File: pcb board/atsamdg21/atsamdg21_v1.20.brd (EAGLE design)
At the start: 100 x 80 mm, 54 parts, among them IC1 DS3231MZ+, IC2 TPS22810TDBVRQ1, SW1 SPST_TACT-KMR2, U1 ATSAMD21G18A-AU, U2 AP2112K-3.3, U4 RFM69HCW, X1 TSW-105-07-G-S, X2 32.768, X3 microUSB, X4 uFL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

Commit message: update 05/15
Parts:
- moved BATTERY 88.5 mm to (3.81, 24.6), turned to 90 degrees
- moved C10 82.8 mm to (9.91, 38.6), turned to 90 degrees
- moved C14 80.6 mm to (12.2, 38.6), turned to 90 degrees
- moved SOLAR 80.0 mm to (3.81, 30.7), turned to 270 degrees
- moved C9 74.2 mm to (54.9, 2.03), turned to 270 degrees
- moved POWER 73.9 mm to (12.2, 47.2), turned to 180 degrees
- moved TRIGGER 69.9 mm to (18.8, 47.2), turned to 180 degrees
- moved R4 69.0 mm to (61.7, 10.4), flipped to the bottom, turned to 270 degrees
- moved C3 62.4 mm to (63.0, 32.3), turned to 270 degrees
- moved IC2 58.3 mm to (42.9, 43.7), turned to 90 degrees
- moved C5 57.5 mm to (52.8, 41.1)
- moved IC1 57.0 mm to (67.1, 10.7), flipped to the bottom, turned to 180 degrees
- moved R7 56.9 mm to (62.0, 26.4), turned to 270 degrees
- moved C1 53.7 mm to (51.8, 38.6), turned to 270 degrees
- moved C7 52.7 mm to (48.8, 24.1)
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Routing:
- net 12VIN: track 0.00 -> 83.2 mm
- net RAIN_G: track 0.00 -> 62.5 mm, vias 0 -> 2
- net A0: track 0.00 -> 58.1 mm, vias 0 -> 1
- net DUETRIG: track 0.00 -> 52.4 mm, vias 0 -> 2
- net D10: track 0.00 -> 48.1 mm
- net D11: track 0.00 -> 42.3 mm
- net USB_D+: track 0.00 -> 38.2 mm, vias 0 -> 2
- net USB_D-: track 0.00 -> 37.8 mm, vias 0 -> 2
- net BATT: track 0.00 -> 34.8 mm
- net N$6: track 0.00 -> 22.9 mm
- net +4V: track 0.00 -> 22.1 mm, vias 0 -> 1
- net SWDIO: track 0.00 -> 20.1 mm
- net TX: track 0.00 -> 19.3 mm, vias 0 -> 1
- net SWCLK: track 0.00 -> 18.5 mm
- net RX: track 0.00 -> 17.4 mm, vias 0 -> 1
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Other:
- board size 100 x 80 mm -> 106.6 x 57.1 mm

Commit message: 05/22 update
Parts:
- moved C11 42.6 mm to (27.2, 11.9), turned to 90 degrees
- moved R10 42.4 mm to (30.2, 10.9)
- moved D1 42.4 mm to (31.2, 8.38)
- moved U2 42.1 mm to (30.2, 14.7)
- moved G1 27.7 mm to (59.9, 12.7), turned to 270 degrees
- moved R4 25.0 mm to (69.1, 34.3), flipped to the top, turned to 0 degrees
- moved C17 23.2 mm to (24.1, 39.6), turned to 270 degrees
- moved C16 23.0 mm to (20.1, 34.3), turned to 90 degrees
- moved IC1 22.7 mm to (64.5, 33.3), flipped to the top, turned to 270 degrees
- moved IC2 22.4 mm to (21.1, 38.6)
- moved SW1 17.6 mm to (49.8, 43.4), turned to 180 degrees
- moved R6 15.0 mm to (33.0, 33.0), turned to 180 degrees
- moved X6 14.0 mm to (57.1, 43.7), turned to 0 degrees
- moved C13 12.4 mm to (45.0, 43.2)
- moved C12 12.4 mm to (45.0, 46.5)
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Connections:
- removed net N$3: R3.2, U1.40
- removed net N$8: C17.1
- net !RESET: now also R3.2, U1.40
- net N$6: now also C17.1
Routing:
- net GND: track 0.00 -> 412.4 mm, vias 0 -> 8
- net +3V3: track 9.57 -> 197.1 mm, vias 0 -> 5
- net VBUS: track 16.6 -> 99.1 mm, vias 0 -> 2
- net N$2: track 0.00 -> 19.3 mm, vias 0 -> 1
- net USB_D+: track 38.2 -> 21.0 mm, vias 2 -> 1
- net USB_D-: track 37.8 -> 21.3 mm, vias 2 -> 1
- net !RESET: track 4.00 -> 16.7 mm, vias 0 -> 2
- net VOLT_SENS: track 12.2 -> 24.6 mm, vias 0 -> 2
- net N$6: track 22.9 -> 12.7 mm
- net D11: track 42.3 -> 33.1 mm, vias 0 -> 2
- net 12VIN: track 83.2 -> 74.9 mm
- net N$7: track 7.90 -> 16.0 mm
- net SCK: track 12.8 -> 4.97 mm
- net RAIN_G: track 62.5 -> 54.8 mm, vias 2 -> 4
- net D10: track 48.1 -> 40.8 mm, vias 0 -> 2
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- added copper zone on layer 1, net GND
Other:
- board size 106.6 x 57.1 mm -> 71.8 x 51.6 mm

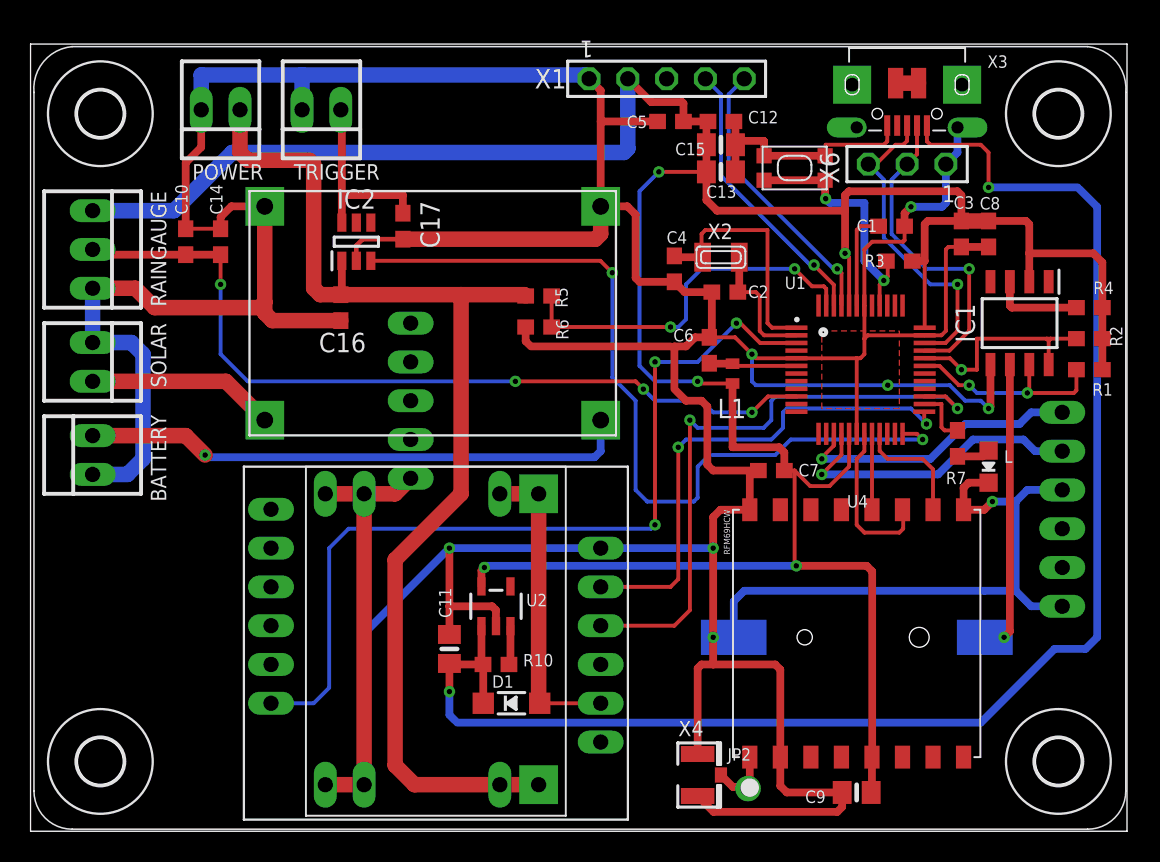
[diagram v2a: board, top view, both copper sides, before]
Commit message: -updated usb pin connections, overlap, ground plane bottom
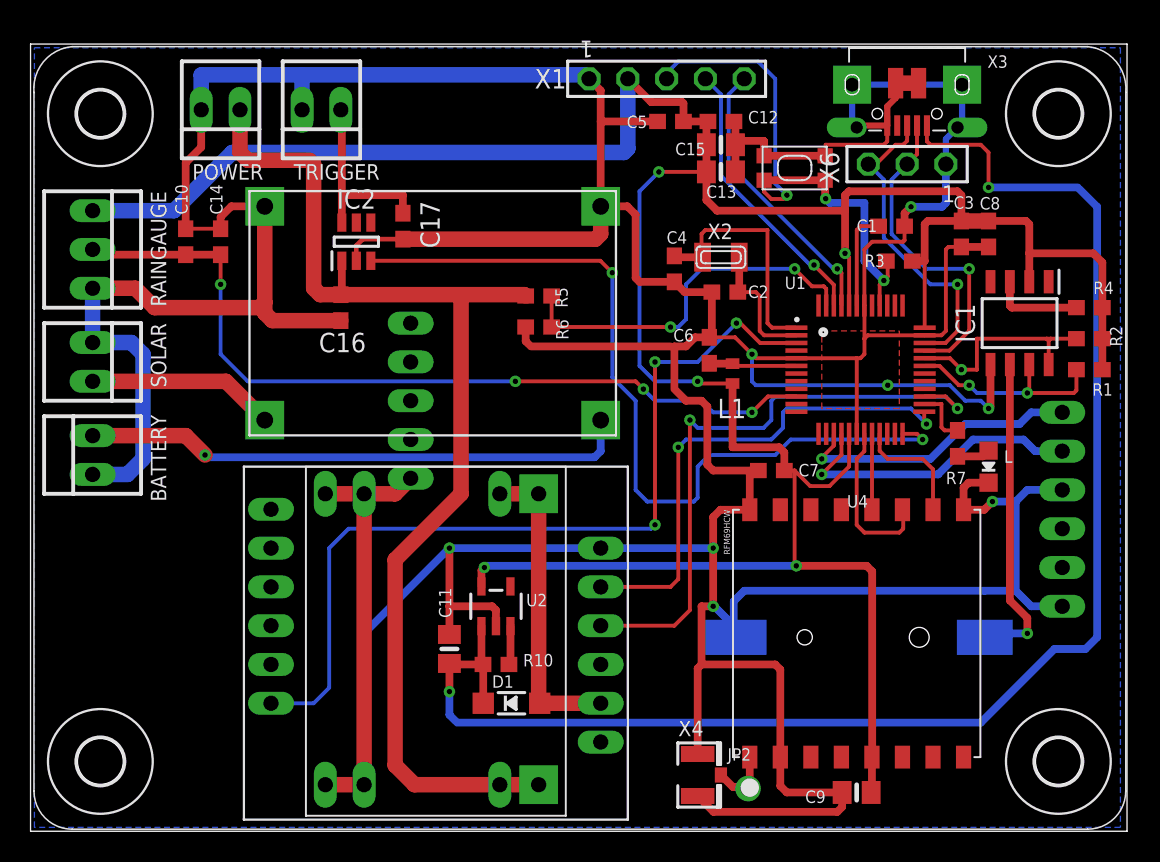
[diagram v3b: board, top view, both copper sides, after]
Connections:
- removed net RST: X1.3
- net !RESET: now also X1.3
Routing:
- net GND: track 412.4 -> 432.6 mm
- net !RESET: track 16.7 -> 35.6 mm, vias 2 -> 3
- net N$2: track 19.3 -> 21.0 mm
- added copper zone on layer 16, net GND
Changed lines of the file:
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@@
 <?xml version="1.0" encoding="utf-8"?>
 <!DOCTYPE eagle SYSTEM "eagle.dtd">
-<eagle version="9.6.1">
+<eagle version="9.5.1">
 <drawing>
 <settings>
@@
 <contactref element="U1" pad="35"/>
 <contactref element="U1" pad="42"/>
-<via x="44.45" y="12.7" extent="1-16" drill="0.35"/>
-<wire x1="44.45" y1="12.7" x2="45.7982" y2="12.7" width="0.254" layer="16"/>
+<via x="44.45" y="14.732" extent="1-16" drill="0.35"/>
+<wire x1="44.45" y1="14.732" x2="44.5282" y2="14.732" width="0.254" layer="16"/>
+<wire x1="45.7982" y1="13.462" x2="44.5282" y2="14.732" width="0.508" layer="16"/>
+<wire x1="45.7982" y1="13.462" x2="45.7982" y2="12.7" width="0.254" layer="16"/>
 <wire x1="49.902" y1="30.976" x2="47.256" y2="30.976" width="0.254" layer="1"/>
 <wire x1="45.886" y1="32.346" x2="44.45" y2="32.346" width="0.254" layer="1"/>
@@
 <wire x1="61.18" y1="22.826" x2="60.848" y2="22.494" width="0.508" layer="1"/>
 <wire x1="48.848" y1="10.588" x2="48.514" y2="10.922" width="0.508" layer="1"/>
-<wire x1="48.514" y1="10.922" x2="44.45" y2="10.922" width="0.508" layer="1"/>
-<wire x1="44.45" y1="10.922" x2="43.688" y2="10.922" width="0.508" layer="1"/>
+<wire x1="48.514" y1="10.922" x2="43.688" y2="10.922" width="0.508" layer="1"/>
 <wire x1="48.848" y1="4.854" x2="48.848" y2="10.588" width="0.508" layer="1"/>
 <wire x1="44.45" y1="20.574" x2="44.45" y2="18.542" width="0.508" layer="1"/>
@@
 <wire x1="59.436" y1="40.894" x2="59.69" y2="41.148" width="0.508" layer="16"/>
 <wire x1="59.69" y1="41.148" x2="59.69" y2="43.688" width="0.508" layer="16"/>
-<wire x1="44.45" y1="18.542" x2="44.45" y2="12.7" width="0.508" layer="1"/>
-<wire x1="44.45" y1="12.7" x2="44.45" y2="10.922" width="0.508" layer="1"/>
+<wire x1="44.45" y1="18.542" x2="44.45" y2="14.732" width="0.508" layer="1"/>
+<wire x1="44.45" y1="14.732" x2="43.688" y2="14.732" width="0.508" layer="1"/>
+<wire x1="43.688" y1="14.732" x2="43.688" y2="10.922" width="0.508" layer="1"/>
 <wire x1="21.082" y1="38.354" x2="21.082" y2="37.358" width="0.3048" layer="1"/>
 <wire x1="24.13" y1="38.774" x2="21.502" y2="38.774" width="0.3048" layer="1"/>
@@
 <wire x1="52.578" y1="1.27" x2="52.898" y2="1.59" width="0.508" layer="1"/>
 <wire x1="52.898" y1="1.59" x2="52.898" y2="2.54" width="0.508" layer="1"/>
-<wire x1="59.69" y1="43.688" x2="60.45" y2="44.448" width="0.508" layer="16"/>
-<wire x1="60.45" y1="44.448" x2="60.45" y2="46.04896875" width="0.508" layer="16"/>
-<wire x1="60.45" y1="46.04896875" x2="60.470515625" y2="46.069484375" width="0.508" layer="16"/>
-<wire x1="60.45" y1="46.09" x2="60.75" y2="48.89" width="0" layer="19" extent="1-1"/>
-<wire x1="60.470515625" y1="46.069484375" x2="60.45" y2="46.09" width="0" layer="19" extent="16-16"/>
-<wire x1="57.9" y1="48.99" x2="60.75" y2="48.89" width="0" layer="19" extent="1-1"/>
-<wire x1="53.55" y1="48.89" x2="56.388" y2="49.002" width="0" layer="19" extent="1-1"/>
-<wire x1="53.85" y1="46.09" x2="53.55" y2="48.89" width="0" layer="19" extent="1-1"/>
-<wire x1="55.85" y1="46.215" x2="53.85" y2="46.09" width="0" layer="19" extent="1-1"/>
+<wire x1="53.55" y1="48.89" x2="53.55" y2="48.768" width="0.4064" layer="16"/>
+<wire x1="53.55" y1="48.768" x2="53.55" y2="46.39" width="0.4064" layer="16"/>
+<wire x1="53.55" y1="46.39" x2="53.85" y2="46.09" width="0.4064" layer="16"/>
+<wire x1="55.85" y1="46.215" x2="55.85" y2="47.468" width="0.4064" layer="1"/>
+<wire x1="56.4" y1="48.018" x2="56.4" y2="48.99" width="0.4064" layer="1"/>
+<wire x1="55.85" y1="47.468" x2="56.4" y2="48.018" width="0.4064" layer="1"/>
+<wire x1="55.85" y1="46.215" x2="53.975" y2="46.215" width="0.4064" layer="1"/>
+<wire x1="53.975" y1="46.215" x2="53.85" y2="46.09" width="0.4064" layer="1"/>
+<wire x1="59.69" y1="43.688" x2="59.69" y2="45.33" width="0.4064" layer="16"/>
+<wire x1="59.69" y1="45.33" x2="60.45" y2="46.09" width="0.4064" layer="16"/>
+<wire x1="60.75" y1="48.89" x2="60.75" y2="46.39" width="0.4064" layer="16"/>
+<wire x1="60.75" y1="46.39" x2="60.45" y2="46.09" width="0.4064" layer="16"/>
+<wire x1="60.75" y1="48.89" x2="53.672" y2="48.89" width="0.4064" layer="16"/>
+<wire x1="53.672" y1="48.89" x2="53.55" y2="48.768" width="0.4064" layer="16"/>
+<polygon width="0.2032" layer="16" isolate="0.4064" thermals="no">
+<vertex x="0" y="51.308"/>
+<vertex x="71.12" y="51.308"/>
+<vertex x="71.12" y="0.254"/>
+<vertex x="0" y="0.254"/>
+</polygon>
 </signal>
 <signal name="N$5">
@@
 <wire x1="54.848" y1="2.59" x2="54.798" y2="2.54" width="0.508" layer="1"/>
 </signal>
-<signal name="RST">
-<contactref element="X1" pad="3"/>
-</signal>
 <signal name="A0">
 <contactref element="U$7" pad="RING"/>
@@
 <contactref element="IC1" pad="6"/>
 <contactref element="G1" pad="+"/>
-<via x="63.5" y="12.7" extent="1-16" drill="0.35"/>
-<wire x1="63.5" y1="12.7" x2="62.2395" y2="12.7" width="0.254" layer="16"/>
-<wire x1="63.5" y1="12.7" x2="63.881" y2="13.081" width="0.508" layer="1"/>
-<wire x1="63.881" y1="13.081" x2="63.881" y2="30.562" width="0.508" layer="1"/>
+<via x="65.024" y="12.954" extent="1-16" drill="0.35"/>
+<wire x1="65.024" y1="12.954" x2="62.4935" y2="12.954" width="0.508" layer="16"/>
+<wire x1="62.2395" y1="12.7" x2="62.4935" y2="12.954" width="0.254" layer="16"/>
+<wire x1="65.024" y1="12.954" x2="65.024" y2="13.97" width="0.508" layer="1"/>
+<wire x1="65.024" y1="13.97" x2="63.881" y2="15.113" width="0.508" layer="1"/>
+<wire x1="63.881" y1="15.113" x2="63.881" y2="30.562" width="0.508" layer="1"/>
 </signal>
 <signal name="INTPIN6">
@@
 <wire x1="51.784" y1="41.4566" x2="51.784" y2="42.634" width="0.508" layer="1"/>
 <wire x1="47.784" y1="42.634" x2="51.784" y2="42.634" width="0.508" layer="1"/>
+<contactref element="X1" pad="3"/>
+<wire x1="47.784" y1="42.634" x2="47.784" y2="41.878" width="0.254" layer="1"/>
+<wire x1="48.26" y1="41.402" x2="49.276" y2="41.402" width="0.254" layer="1"/>
+<wire x1="49.276" y1="41.402" x2="49.276" y2="41.656" width="0.254" layer="1"/>
+<via x="49.276" y="41.656" extent="1-16" drill="0.35"/>
+<wire x1="49.276" y1="41.656" x2="48.514" y2="42.418" width="0.254" layer="16"/>
+<wire x1="48.514" y1="42.418" x2="48.514" y2="49.276" width="0.254" layer="16"/>
+<wire x1="48.514" y1="49.276" x2="47.381" y2="50.409" width="0.254" layer="16"/>
+<wire x1="47.381" y1="50.409" x2="42.164" y2="50.409" width="0.254" layer="16"/>
+<wire x1="42.164" y1="50.409" x2="41.402" y2="49.647" width="0.254" layer="16"/>
+<wire x1="41.402" y1="49.647" x2="41.402" y2="49.276" width="0.254" layer="16"/>
+<wire x1="47.784" y1="41.878" x2="48.26" y2="41.402" width="0.254" layer="1"/>
 </signal>
 <signal name="12VIN">
@@
 <contactref element="U$7" pad="VCC"/>
 <wire x1="33.092" y1="8.382" x2="33.274" y2="8.382" width="0.254" layer="1"/>
-<wire x1="33.274" y1="8.382" x2="37.084" y2="8.382" width="0.254" layer="1"/>
+<wire x1="33.274" y1="8.382" x2="37.084" y2="8.382" width="1.016" layer="1"/>
 <wire x1="33.02" y1="8.89" x2="33.02" y2="8.636" width="0.254" layer="1"/>
 <wire x1="33.02" y1="8.636" x2="33.274" y2="8.382" width="0.254" layer="1"/>

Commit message: update 05/29
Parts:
- added U$24: (no value), logo:LOGO_SML_TNAME
- turned BATTERY to 270 degrees
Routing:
- net GND: track 432.6 -> 429.7 mm
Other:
- board text added: "v1.0 TP"

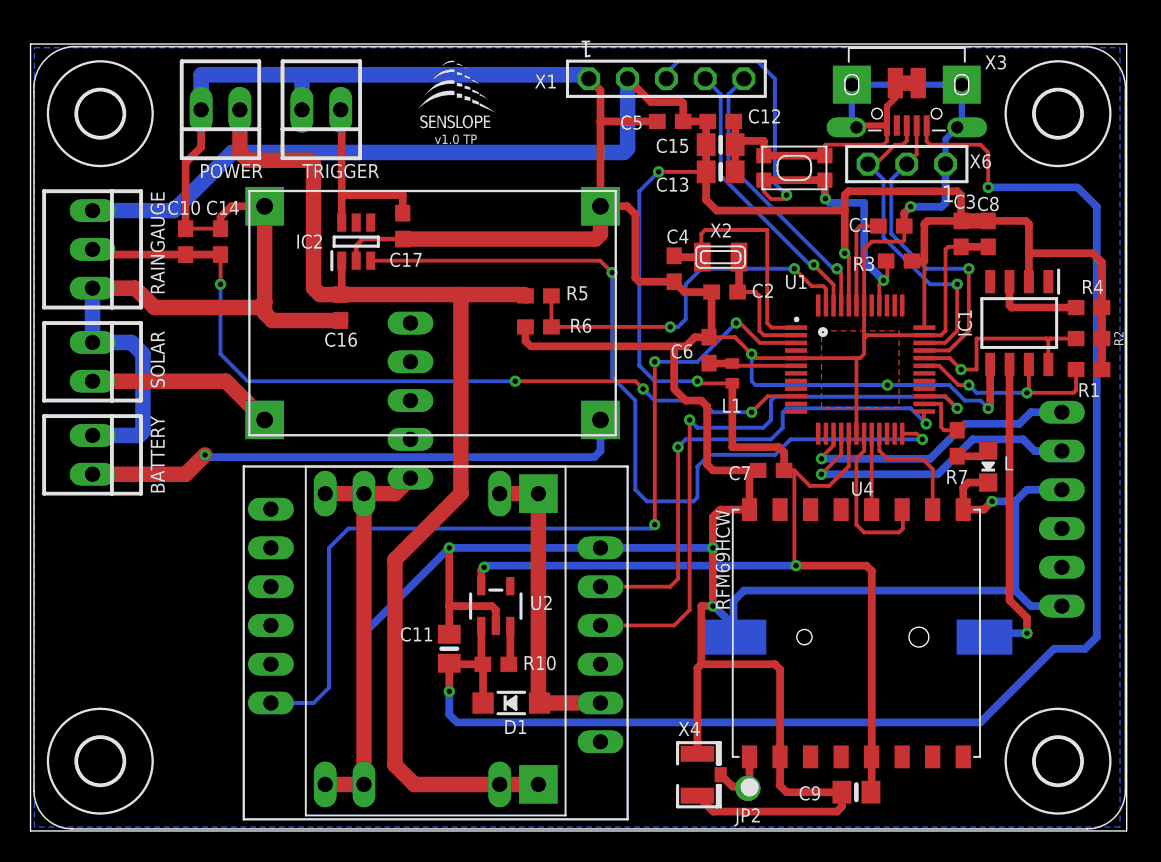
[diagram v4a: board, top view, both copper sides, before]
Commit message: -added gsm ring functions -updated routing
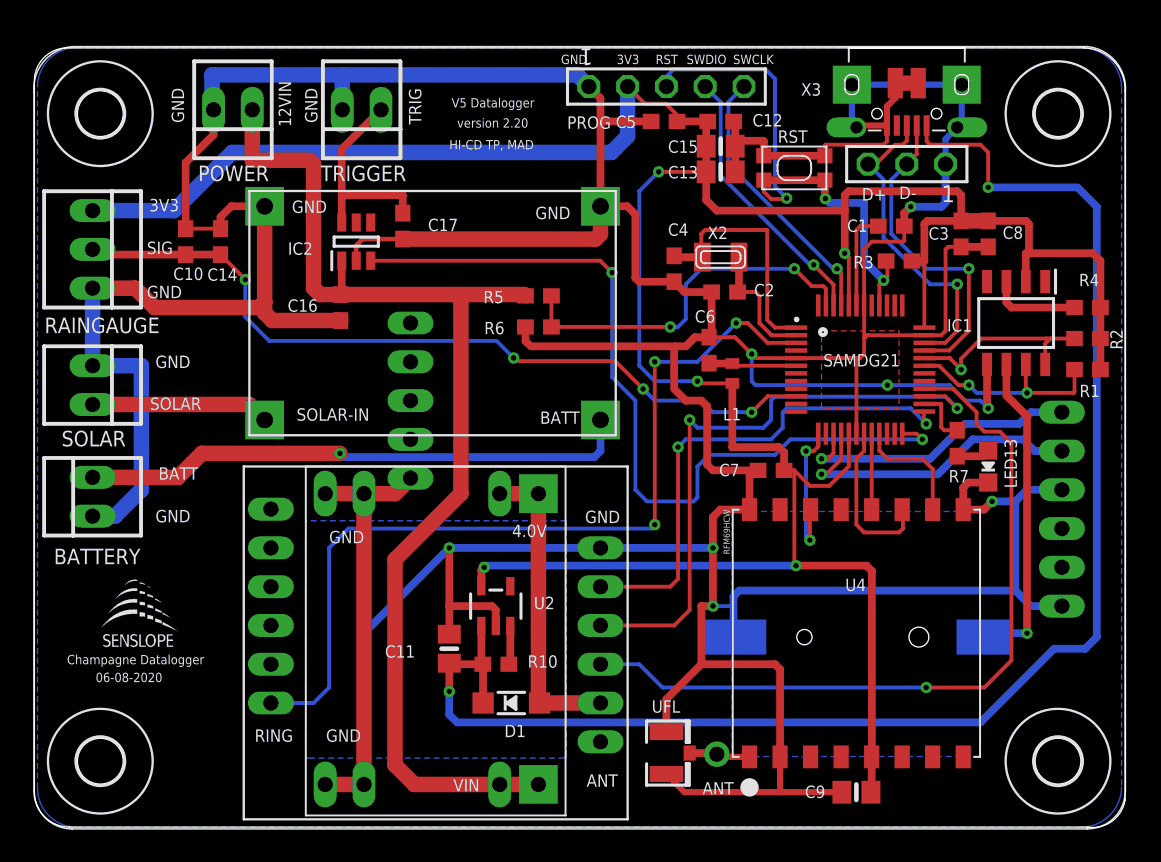
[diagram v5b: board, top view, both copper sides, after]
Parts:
- removed JP2: (no value), microbuilder:1X01_ROUND
- removed X1: TSW-105-07-G-S, con-samtec:TSW-105-XX-G-S
- removed X4: uFL, microbuilder:U.FL
- added ANT: (no value), microbuilder:1X01_ROUND
- added PROG: TSW-105-07-G-S, con-samtec:TSW-105-XX-G-S
- added UFL: uFL, microbuilder:U.FL
- moved U$24 39.8 mm to (6.68, 13.7)
- moved BATTERY 2.74 mm to (3.81, 21.9), turned to 90 degrees
- moved TRIGGER 2.64 mm to (21.4, 47.2)
- moved SOLAR 1.52 mm to (3.81, 29.2)
- moved POWER 0.81 mm to (13.0, 47.2)
- moved C5 0.41 mm to (41.2, 46.5)
- moved IC1 0.20 mm to (64.3, 33.3)
- moved C15 0.10 mm to (45.0, 44.9)
- moved R1 0.10 mm to (69.0, 30.2)
- moved R2 0.10 mm to (69.0, 32.3)
- moved R4 0.10 mm to (69.0, 34.3)
- renumbered G1 to RTC-BATT, L to LED13, U1 to SAMDG21, X6 to RST
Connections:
- removed net D12: SAMDG21.28
- removed net RST_D4: SAMDG21.13
- new net GSM_RST: SAMDG21.28, U$7.RST
- net !RESET: now also PROG.3; no longer X1.3
- net +3V3: now also PROG.2; no longer X1.2
- net ANT: now also ANT.1, UFL.3; no longer JP2.1, X4.3
- net D4_RST: now also SAMDG21.13
- net GND: now also PROG.1, UFL.1, UFL.2; no longer X1.1, X4.1, X4.2
- net SWCLK: now also PROG.5; no longer X1.5
- net SWDIO: now also PROG.4; no longer X1.4
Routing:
- net GSM_RST: track 0.00 -> 50.1 mm, vias 0 -> 1
- net D4_RST: track 0.00 -> 9.74 mm, vias 0 -> 2
- net RAIN_G: track 54.8 -> 52.4 mm
- net +3V3: track 197.1 -> 195.7 mm
- net GND: track 429.7 -> 431.0 mm
- net N$6: track 12.7 -> 13.7 mm
- net SCL: track 14.2 -> 13.4 mm
- net SOLAR: track 12.3 -> 11.7 mm
- net 12VIN: track 74.9 -> 74.4 mm
- net SWCLK: track 18.5 -> 18.0 mm
- net SWDIO: track 18.5 -> 18.0 mm
- added copper zone on layer 16, net DC-CUT
- added copper zone on layer 16, net LORA-CUT
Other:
- board size 71.8 x 51.6 mm -> 71.5 x 51.1 mm
- board text added: "06-08-2020"
- board text added: "12VIN"
- board text added: "3V3"
- board text added: "4.0V"
- board text added: "ANT"
- board text added: "BATT"
- board text added: "Champagne Datalogger"
- board text added: "D+"
- board text added: "D-"
- board text added: "GND"
- board text added: "HI-CD TP, MAD"
- board text added: "RING"
- board text added: "RST"
- board text added: "SIG"
- board text added: "SOLAR"
- board text added: "SOLAR-IN"
- board text added: "SWCLK"
- board text added: "SWDIO"
- board text added: "TRIG"
- board text added: "V5 Datalogger"
- board text added: "VIN"
- board text added: "version 2.20"
- board text removed: "v1.0 TP"
